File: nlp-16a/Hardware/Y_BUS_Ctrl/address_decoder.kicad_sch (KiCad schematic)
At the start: 2 parts, among them U41 CD74HC00, U42 CD74HC00

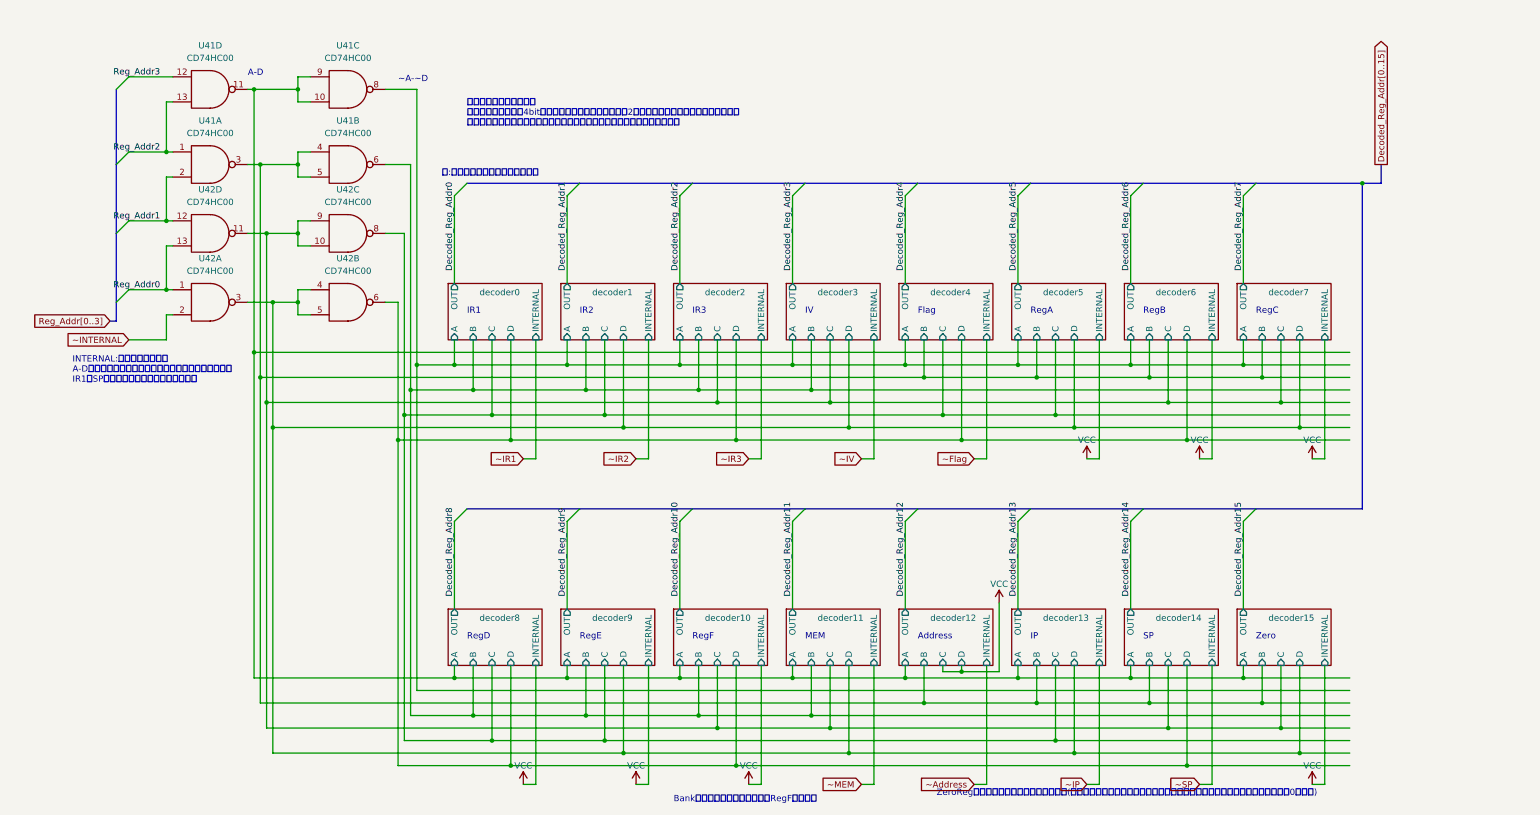
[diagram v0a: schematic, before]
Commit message: TMPレジスタ等を追加
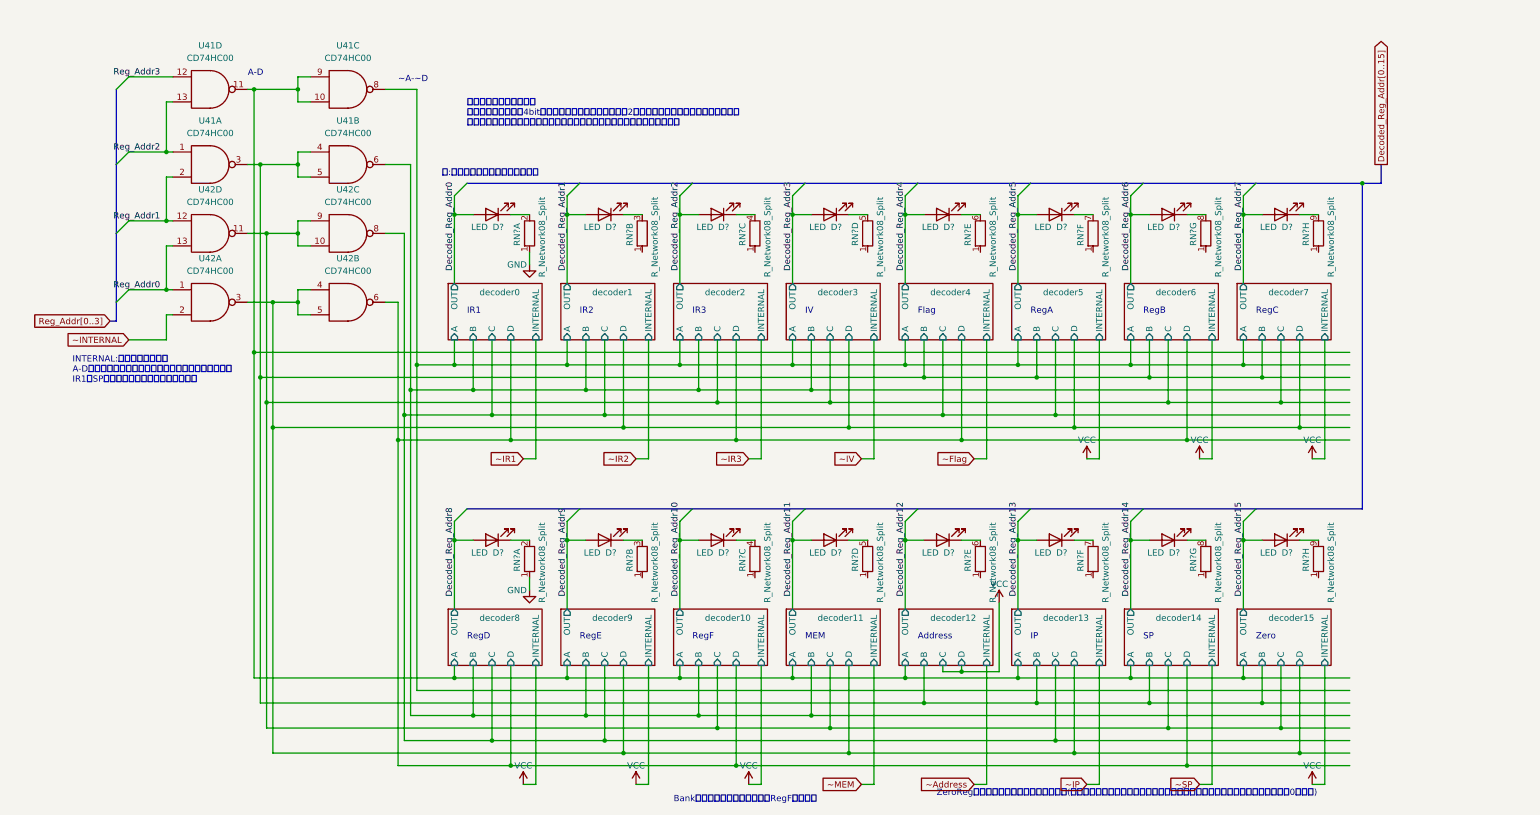
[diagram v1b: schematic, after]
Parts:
- added D? (x16): LED, symbol Device:LED
- added RN? (x16): R_Network08_Split, Resistor_THT:R_Array_SIP9, symbol Device:R_Network08_Split
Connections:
- net Decoded_Reg_Addr0: now also D?.2 (A)
- net Decoded_Reg_Addr1: now also D?.2 (A)
- net Decoded_Reg_Addr10: now also D?.2 (A)
- net Decoded_Reg_Addr11: now also D?.2 (A)
- net Decoded_Reg_Addr12: now also D?.2 (A)
- net Decoded_Reg_Addr13: now also D?.2 (A)
- net Decoded_Reg_Addr14: now also D?.2 (A)
- net Decoded_Reg_Addr15: now also D?.2 (A)
- net Decoded_Reg_Addr2: now also D?.2 (A)
- net Decoded_Reg_Addr3: now also D?.2 (A)
- net Decoded_Reg_Addr4: now also D?.2 (A)
- net Decoded_Reg_Addr5: now also D?.2 (A)
- net Decoded_Reg_Addr6: now also D?.2 (A)
- net Decoded_Reg_Addr7: now also D?.2 (A)
- net Decoded_Reg_Addr8: now also D?.2 (A)
- net Decoded_Reg_Addr9: now also D?.2 (A)
- net GND: now also RN?.1 (R1.1), RN?.1 (R1.1)
- new net: D?.1 (K), RN?.6 (R5.2) (x2)
- new net: D?.1 (K), RN?.4 (R3.2) (x2)
- new net: D?.1 (K), RN?.3 (R2.2) (x2)
- new net: D?.1 (K), RN?.7 (R6.2) (x2)
- new net: D?.1 (K), RN?.9 (R8.2) (x2)
- new net: D?.1 (K), RN?.2 (R1.2) (x2)
- new net: D?.1 (K), RN?.8 (R7.2) (x2)
- new net: D?.1 (K), RN?.5 (R4.2) (x2)

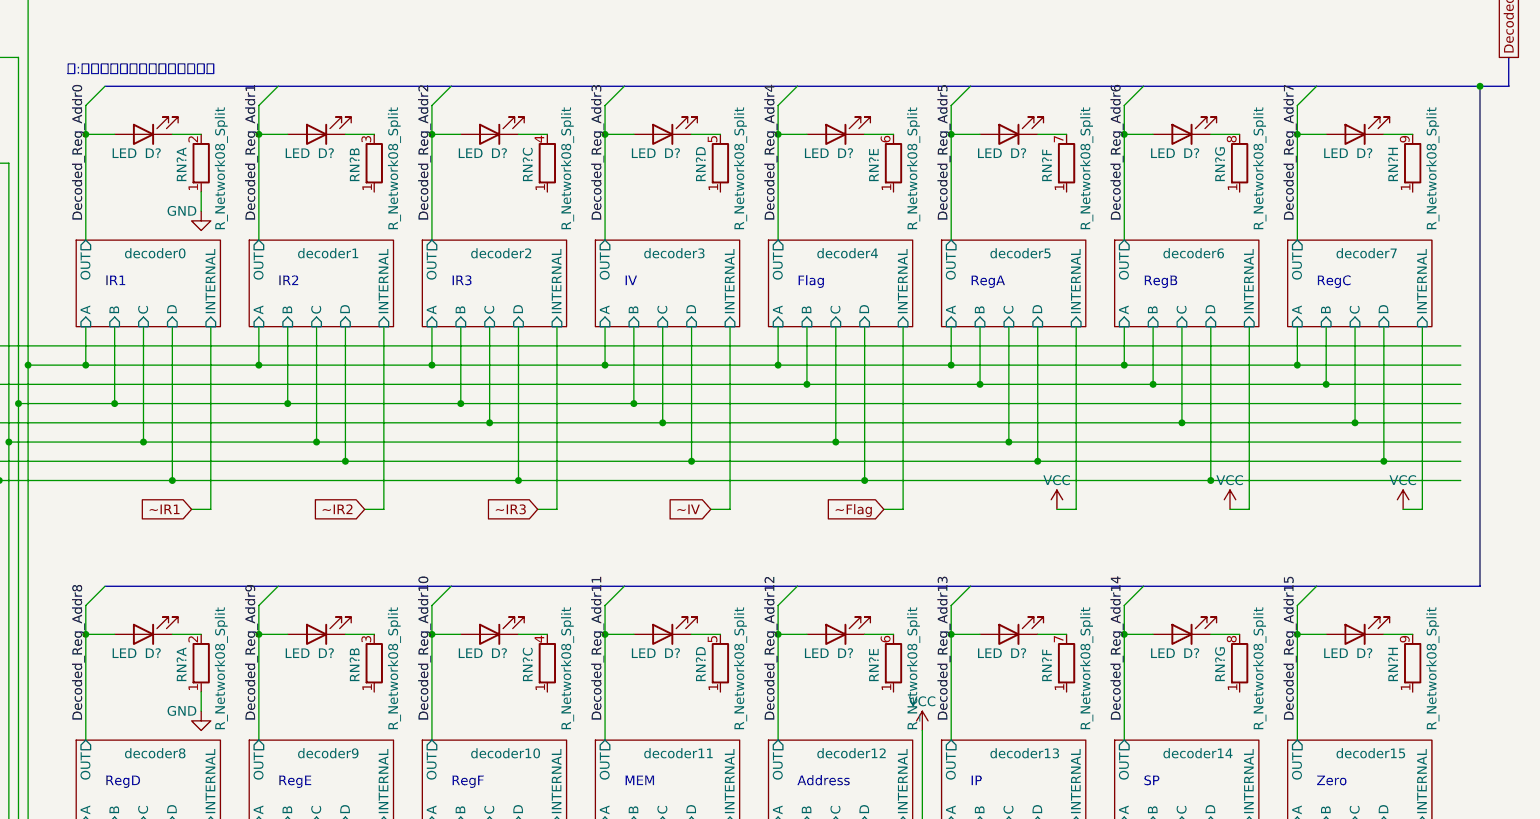
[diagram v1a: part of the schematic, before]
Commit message: Yバス制御 配置の決定，リファレンスの割り当て，ERCの確認完了
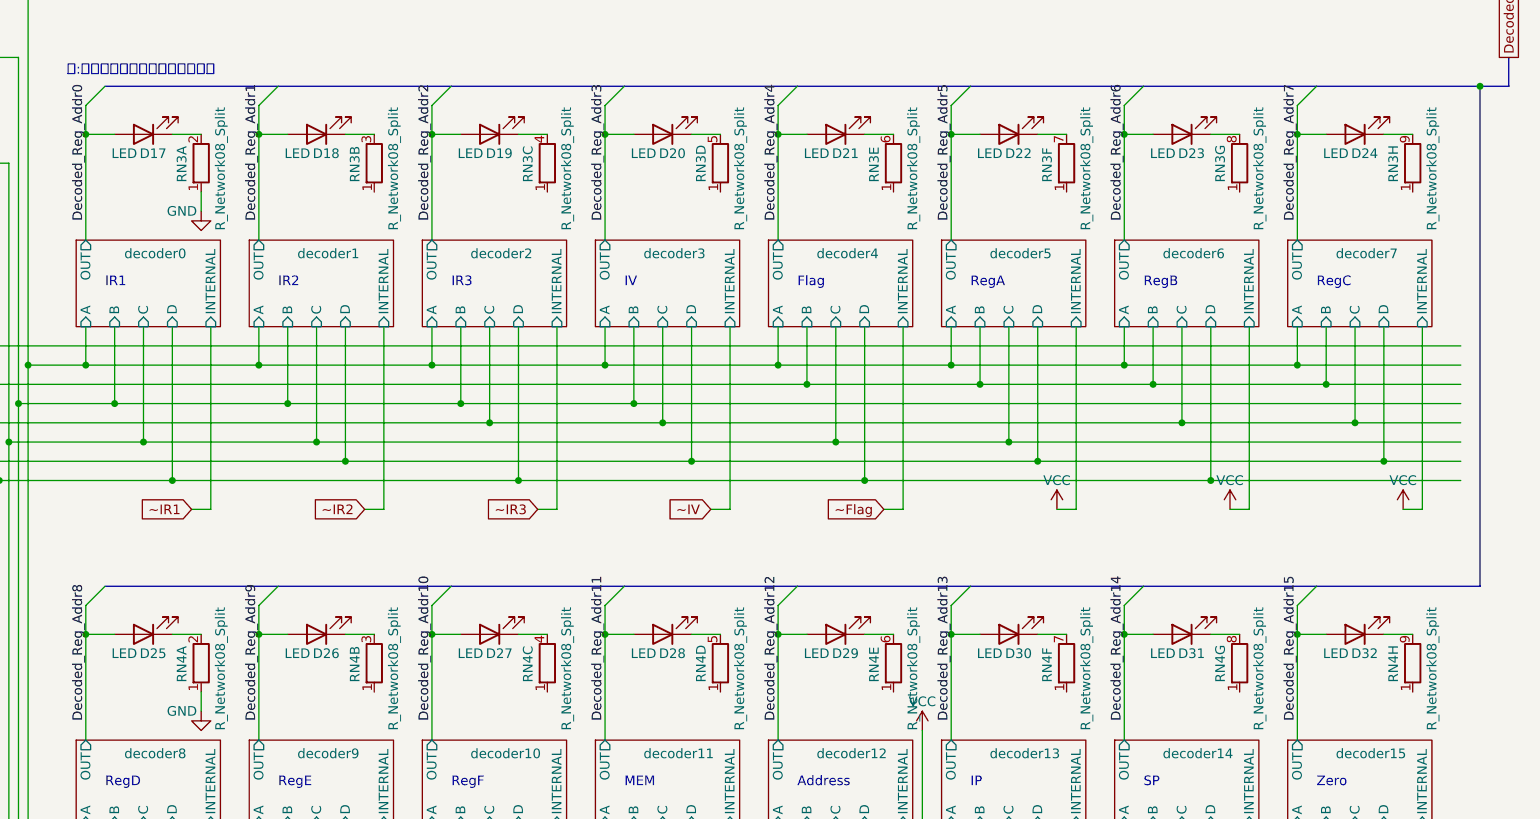
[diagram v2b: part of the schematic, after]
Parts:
- gave numbers to parts that had none: 18
